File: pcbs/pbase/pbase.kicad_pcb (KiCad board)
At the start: 2 copper layers, 100 x 100 mm, 50 parts, among them J1 SD_Card, J2 Conn_01x04, J3 Conn_01x04, M3 MountingHole_3.2mm_M3_DIN965, U1 LPCXpresso_LPC1769_revB, U2 acc_mpu9250_board, U3 GPS_EM506

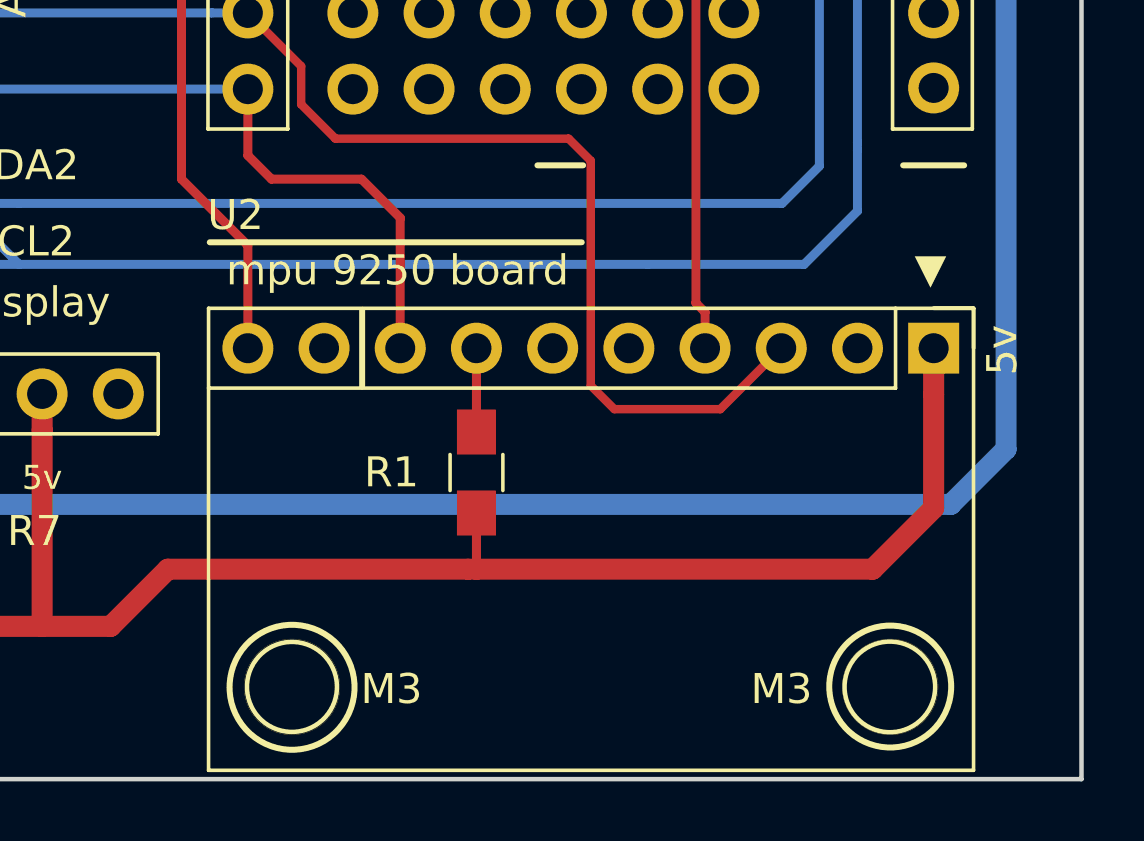
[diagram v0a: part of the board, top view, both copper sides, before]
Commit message: cambiado footprint acc mpu9250, agregado mounting hole para mpu 6050
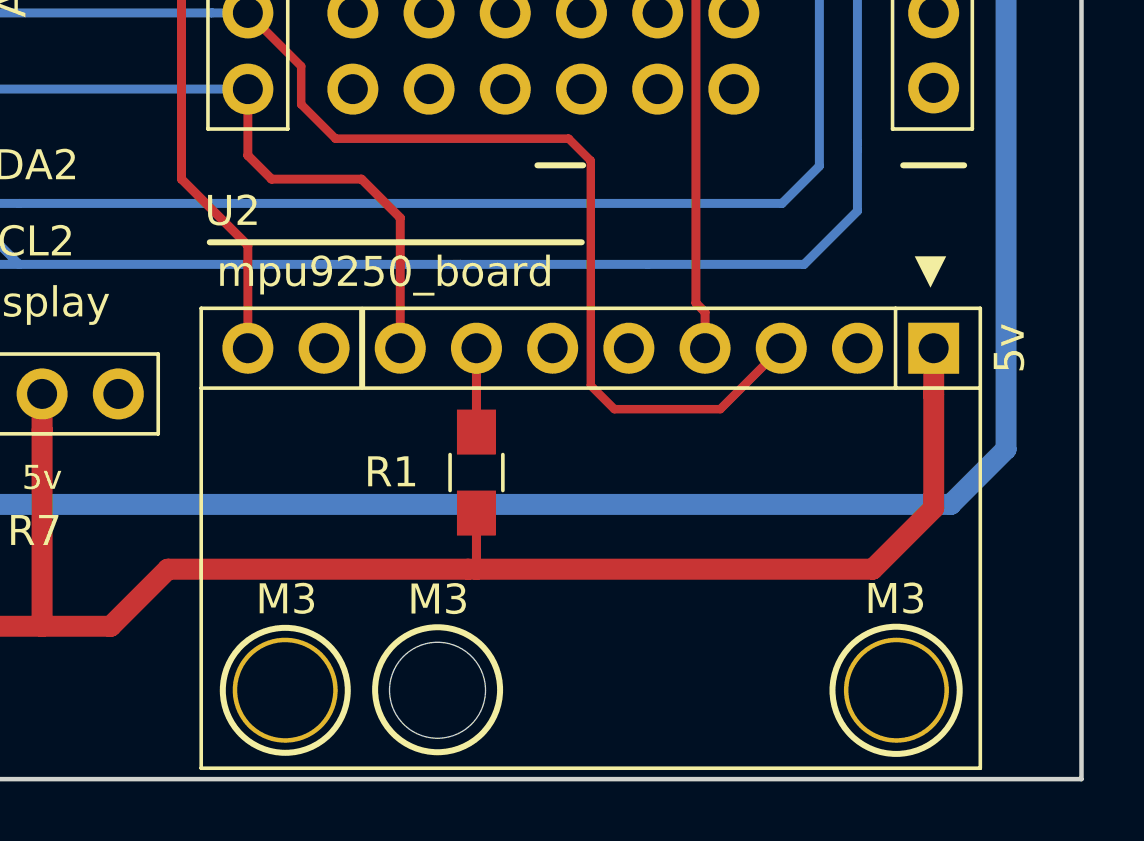
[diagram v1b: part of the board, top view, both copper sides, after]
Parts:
- added M3: MountingHole_3.2mm_M3_DIN965, Mounting_Holes:MountingHole_3.2mm_M3_DIN965, F.Cu at (178.5, 147.0)

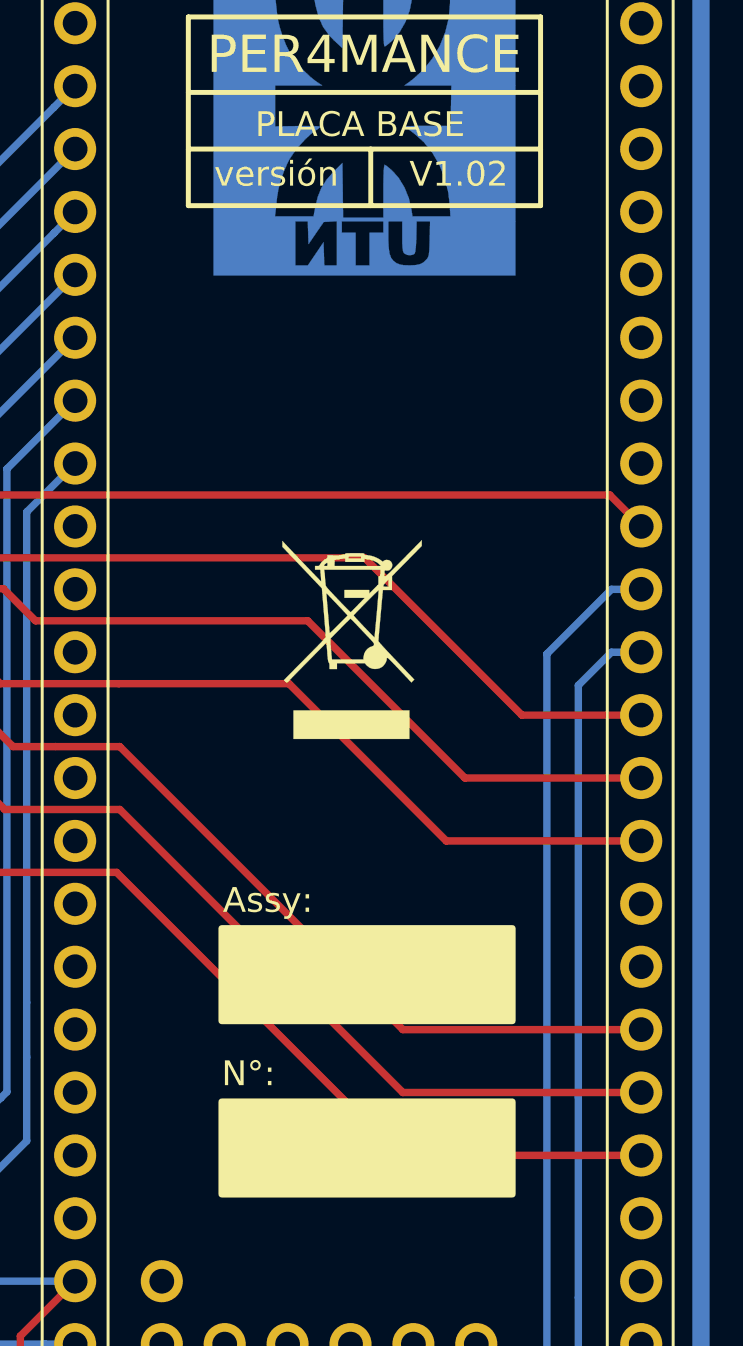
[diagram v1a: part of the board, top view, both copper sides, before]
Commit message: pcb lpc finalizado sin llaves
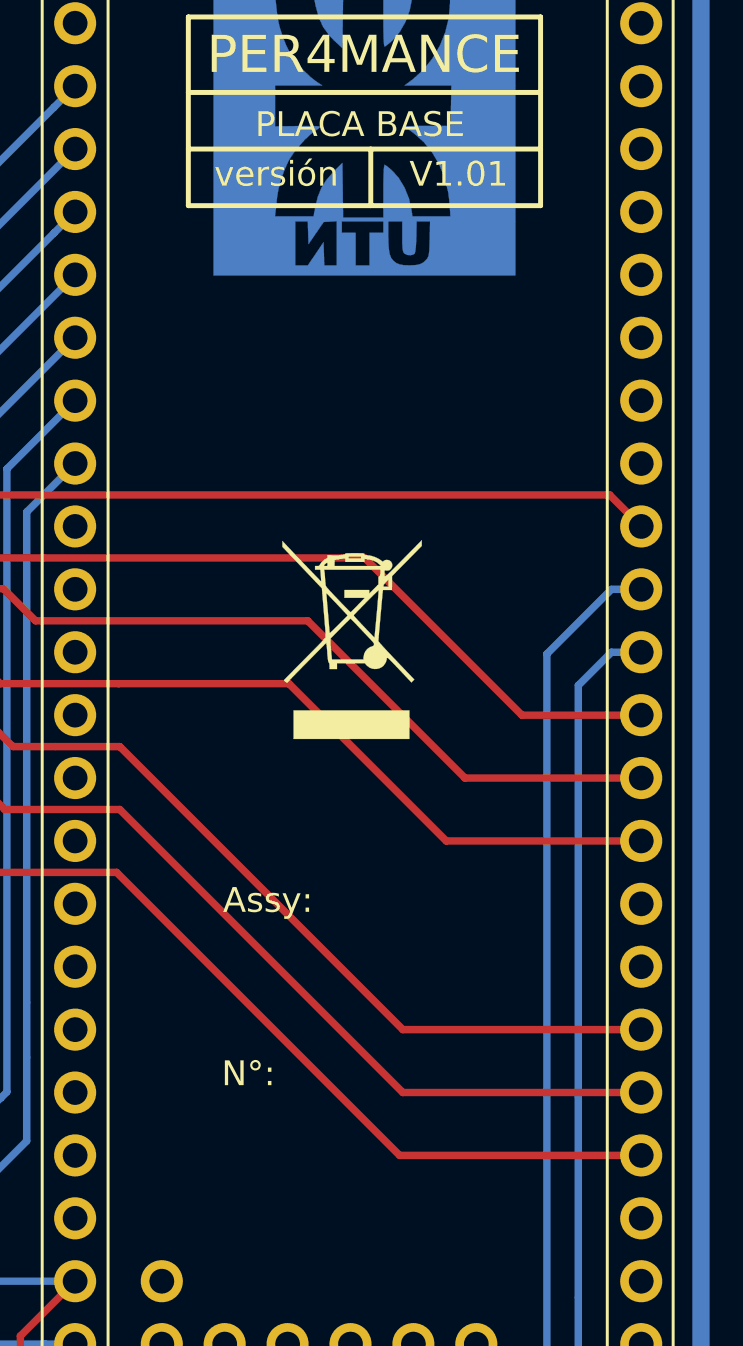
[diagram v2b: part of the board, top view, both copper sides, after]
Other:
- board text added: "V1.01"
- board text removed: "V1.02"
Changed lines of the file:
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@@
     (links 99)
     (no_connects 0)
-    (area 99.924999 49.924999 200.075001 150.075001)
+    (area 84.864287 2.605 430.999997 172.700001)
     (thickness 1.6)
     (drawings 133)
@@
     (effects (font (size 1 1) (thickness 0.25)))
   )
-  (gr_text V1.02 (at 187.706 74.676) (layer F.SilkS)
+  (gr_text V1.01 (at 187.706 74.676) (layer F.SilkS)
     (effects (font (size 1 1) (thickness 0.25)))
   )
@@
     (connect_pads (clearance 0.508))
     (min_thickness 0.254)
-    (fill yes (arc_segments 16) (thermal_gap 0.508) (thermal_bridge_width 0.508))
+    (fill (arc_segments 16) (thermal_gap 0.508) (thermal_bridge_width 0.508))
     (polygon
       (pts
@@
     (connect_pads (clearance 0.508))
     (min_thickness 0.254)
-    (fill yes (arc_segments 16) (thermal_gap 0.508) (thermal_bridge_width 0.508))
+    (fill (arc_segments 16) (thermal_gap 0.508) (thermal_bridge_width 0.508))
     (polygon
       (pts
@@
     (connect_pads (clearance 0.508))
     (min_thickness 0.254)
-    (fill yes (arc_segments 16) (thermal_gap 0.508) (thermal_bridge_width 0.508))
+    (fill (arc_segments 16) (thermal_gap 0.508) (thermal_bridge_width 0.508))
     (polygon
       (pts
@@
     (connect_pads (clearance 0.508))
     (min_thickness 0.254)
-    (fill yes (arc_segments 16) (thermal_gap 0.508) (thermal_bridge_width 0.508))
+    (fill (arc_segments 16) (thermal_gap 0.508) (thermal_bridge_width 0.508))
     (polygon
       (pts
@@
     (connect_pads (clearance 0.508))
     (min_thickness 0.254)
-    (fill yes (arc_segments 16) (thermal_gap 0.508) (thermal_bridge_width 0.508))
+    (fill (arc_segments 16) (thermal_gap 0.508) (thermal_bridge_width 0.508))
     (polygon
       (pts
@@
     (connect_pads (clearance 0.508))
     (min_thickness 0.254)
-    (fill yes (arc_segments 16) (thermal_gap 0.508) (thermal_bridge_width 0.508))
+    (fill (arc_segments 16) (thermal_gap 0.508) (thermal_bridge_width 0.508))
     (polygon
       (pts

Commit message: PCBs pbase y pbase-ino FINALIZADOS, archivos gerbers en zip dentro del directrio /pcbs
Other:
- board text added: "Ailu"
- board text removed: "DUDA: - Puedo poner a parte de la SD los resistores en bottom?? Esto facilitaria el routeo y reduciria el uso de vias. - Las vias que use ahí están bien? Traería problemas?"
- board text removed: "DUDA: correcto el tamaño de la VIA?"
- board text removed: "Dice Ridolfi que para I2C como es lento no hay problema. Lo mismo pasa con SPI. USB Si trae problemas."
- board text removed: "GRID 20 MILS: - RES SMD - CAPS SMD - SD - TPs INTERMEDIOS EL RESTO CON 1MM"
- board text removed: "Grid: 20 mils para PLACING"
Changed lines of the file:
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@@
     (links 99)
     (no_connects 0)
-    (area 84.864287 2.605 430.999997 172.700001)
+    (area 84.864287 38.8 252.142857 172.700001)
     (thickness 1.6)
-    (drawings 133)
+    (drawings 129)
     (tracks 524)
     (zones 0)
@@
     (39 F.Mask user)
     (40 Dwgs.User user)
-    (41 Cmts.User user hide)
+    (41 Cmts.User user)
     (42 Eco1.User user)
     (43 Eco2.User user)
@@
     (pad_drill 3.2)
     (pad_to_mask_clearance 0.2)
-    (aux_axis_origin 120 145)
+    (aux_axis_origin 113 145)
     (visible_elements 7FFFFFFF)
     (pcbplotparams
-      (layerselection 0x00030_80000001)
+      (layerselection 0x010fc_80000001)
       (usegerberextensions false)
       (excludeedgelayer true)
@@
       (psa4output false)
       (plotreference true)
-      (plotvalue true)
+      (plotvalue false)
       (plotinvisibletext false)
       (padsonsilk false)
@@
       (drillshape 0)
       (scaleselection 1)
-      (outputdirectory ""))
+      (outputdirectory gerbers/))
   )
   (net 0 "")
@@
     (pad 1 np_thru_hole circle (at 0 0) (size 3.2 3.2) (drill 3.2) (layers *.Cu *.Mask))
   )
+  (gr_text Ailu (at 188 147) (layer B.Cu)
+    (effects (font (size 1 1) (thickness 0.25)) (justify mirror))
+  )
   (gr_circle (center 178.5366 147.02028) (end 180.6194 147.04568) (layer F.SilkS) (width 0.2))
   (gr_text "Material: FR4\nCopper Weight: 1oz / 35um\nPCB SIZE: 100 X 100 mm\nPCB COLOR: RED\n" (at 220 60) (layer Cmts.User)
@@
     (effects (font (size 1 1) (thickness 0.25)))
   )
-  (gr_text "DUDA:\n- Puedo poner a parte de la SD los resistores en bottom?? Esto facilitaria el routeo y reduciria el uso de vias.\n- Las vias que use ahí están bien? Traería problemas?" (at 300 80) (layer Dwgs.User)
-    (effects (font (size 1.5 1.5) (thickness 0.3)) (justify left))
-  )
   (dimension 47 (width 0.3) (layer Dwgs.User)
     (gr_text "47,000 mm" (at 128.5 171.35) (layer Dwgs.User)
@@
     (arrow2b (pts (xy 142.3346 118.944918) (xy 141.747234 117.818907)))
   )
-  (gr_text "DUDA:\ncorrecto el tamaño de la VIA?" (at 300.0502 71.8312) (layer Dwgs.User)
-    (effects (font (size 1.5 1.5) (thickness 0.3)) (justify left))
-  )
   (gr_text "GND\n" (at 151.384 137.668) (layer F.SilkS)
     (effects (font (size 1 1) (thickness 0.25)))
@@
     (effects (font (size 1 1) (thickness 0.25)))
   )
-  (gr_text "GRID 20 MILS:\n- RES SMD\n- CAPS SMD\n- SD\n- TPs INTERMEDIOS\n\nEL RESTO CON 1MM" (at 300 58) (layer Dwgs.User)
-    (effects (font (size 1.5 1.5) (thickness 0.3)) (justify left))
-  )
   (gr_line (start 157 140) (end 157 130) (layer F.SilkS) (width 0.25))
   (gr_line (start 157 100) (end 157 97) (layer F.SilkS) (width 0.25))
@@
   (gr_line (start 100 150) (end 200 150) (layer Edge.Cuts) (width 0.15))
   (gr_line (start 100 50) (end 100 150) (layer Edge.Cuts) (width 0.15))
-  (gr_text "Dice Ridolfi que para I2C como es lento no hay problema.\nLo mismo pasa con SPI.\nUSB Si trae problemas." (at 299.72 25.4) (layer Dwgs.User)
-    (effects (font (size 1.5 1.5) (thickness 0.3)) (justify left))
-  )
-  (gr_text "Grid:\n20 mils para PLACING\n" (at 299.72 5.08) (layer Dwgs.User)
-    (effects (font (size 1.5 1.5) (thickness 0.3)) (justify left))
-  )
   (segment (start 195.072 60.96) (end 197.485 63.373) (width 0.7) (layer B.Cu) (net 1))
   (segment (start 197.485 63.373) (end 197.485 139.0015) (width 0.7) (layer B.Cu) (net 1))
@@
     (connect_pads (clearance 0.508))
     (min_thickness 0.254)
-    (fill (arc_segments 16) (thermal_gap 0.508) (thermal_bridge_width 0.508))
+    (fill yes (arc_segments 16) (thermal_gap 0.508) (thermal_bridge_width 0.508))
     (polygon
       (pts
@@
     (connect_pads (clearance 0.508))
     (min_thickness 0.254)
-    (fill (arc_segments 16) (thermal_gap 0.508) (thermal_bridge_width 0.508))
+    (fill yes (arc_segments 16) (thermal_gap 0.508) (thermal_bridge_width 0.508))
     (polygon
       (pts
@@
     (connect_pads (clearance 0.508))
     (min_thickness 0.254)
-    (fill (arc_segments 16) (thermal_gap 0.508) (thermal_bridge_width 0.508))
+    (fill yes (arc_segments 16) (thermal_gap 0.508) (thermal_bridge_width 0.508))
     (polygon
       (pts
@@
     (connect_pads (clearance 0.508))
     (min_thickness 0.254)
-    (fill (arc_segments 16) (thermal_gap 0.508) (thermal_bridge_width 0.508))
+    (fill yes (arc_segments 16) (thermal_gap 0.508) (thermal_bridge_width 0.508))
     (polygon
       (pts
@@
     (connect_pads (clearance 0.508))
     (min_thickness 0.254)
-    (fill (arc_segments 16) (thermal_gap 0.508) (thermal_bridge_width 0.508))
+    (fill yes (arc_segments 16) (thermal_gap 0.508) (thermal_bridge_width 0.508))
     (polygon
       (pts
@@
     (connect_pads (clearance 0.508))
     (min_thickness 0.254)
-    (fill (arc_segments 16) (thermal_gap 0.508) (thermal_bridge_width 0.508))
+    (fill yes (arc_segments 16) (thermal_gap 0.508) (thermal_bridge_width 0.508))
     (polygon
       (pts

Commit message: pdfs realizados
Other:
- board text added: "!"
- board text added: "IMPORTANTE. - Todos los resistores y C2 son 0805. C1: CP_Tantalum_Case-A_EIA-3216-18. - Conector del GPS: JST_SH_SM06B-SRSS-TB_06x1.00mm_Angled. - Tarjeta SD: SD Oupiin 9004-BA09W01C00A - Resistores de PULL-UP: R6 y R7 deben calcularse para realizar la comunicación I2C del display. Si alguno de los dos dispositivos ya los incorpora, quitarlos, no pasa nada. - R1 Puede no conectarse. En este caso 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"
- board text added: "PRECAUCIÓN: NO PROGRAMAR SI LA PLACA ESTÁ ALIMENTADA EXTERNAMENTE. ES ALTAMENTE RECOMENDABLE PROGRAMAR EL MICROCONTROLADOR POR SEPARADO ANTES DE CONECTARLO A ESTA PLACA. RIESGO DE QUEMAR TODO."
- board text added: "Placa Base"
- board text added: "Valores: R1 = 0R (opcional) R2 = 10K R3 = 10K R4 = 33K R5 = 33K R6 = calcular R7 = calcular C1 = 1uF x 16V (polarizado) C2 = 100nF"
